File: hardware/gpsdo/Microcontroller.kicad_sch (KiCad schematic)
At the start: 31 parts, among them J1 Conn_01x02, J2 Conn_02x03_Top_Bottom, J3 USB_C_Receptacle_USB2.0_14P, U6 STM32F411CEUx, U7 AMS1117-3.3, X1 X322516MLB4SI

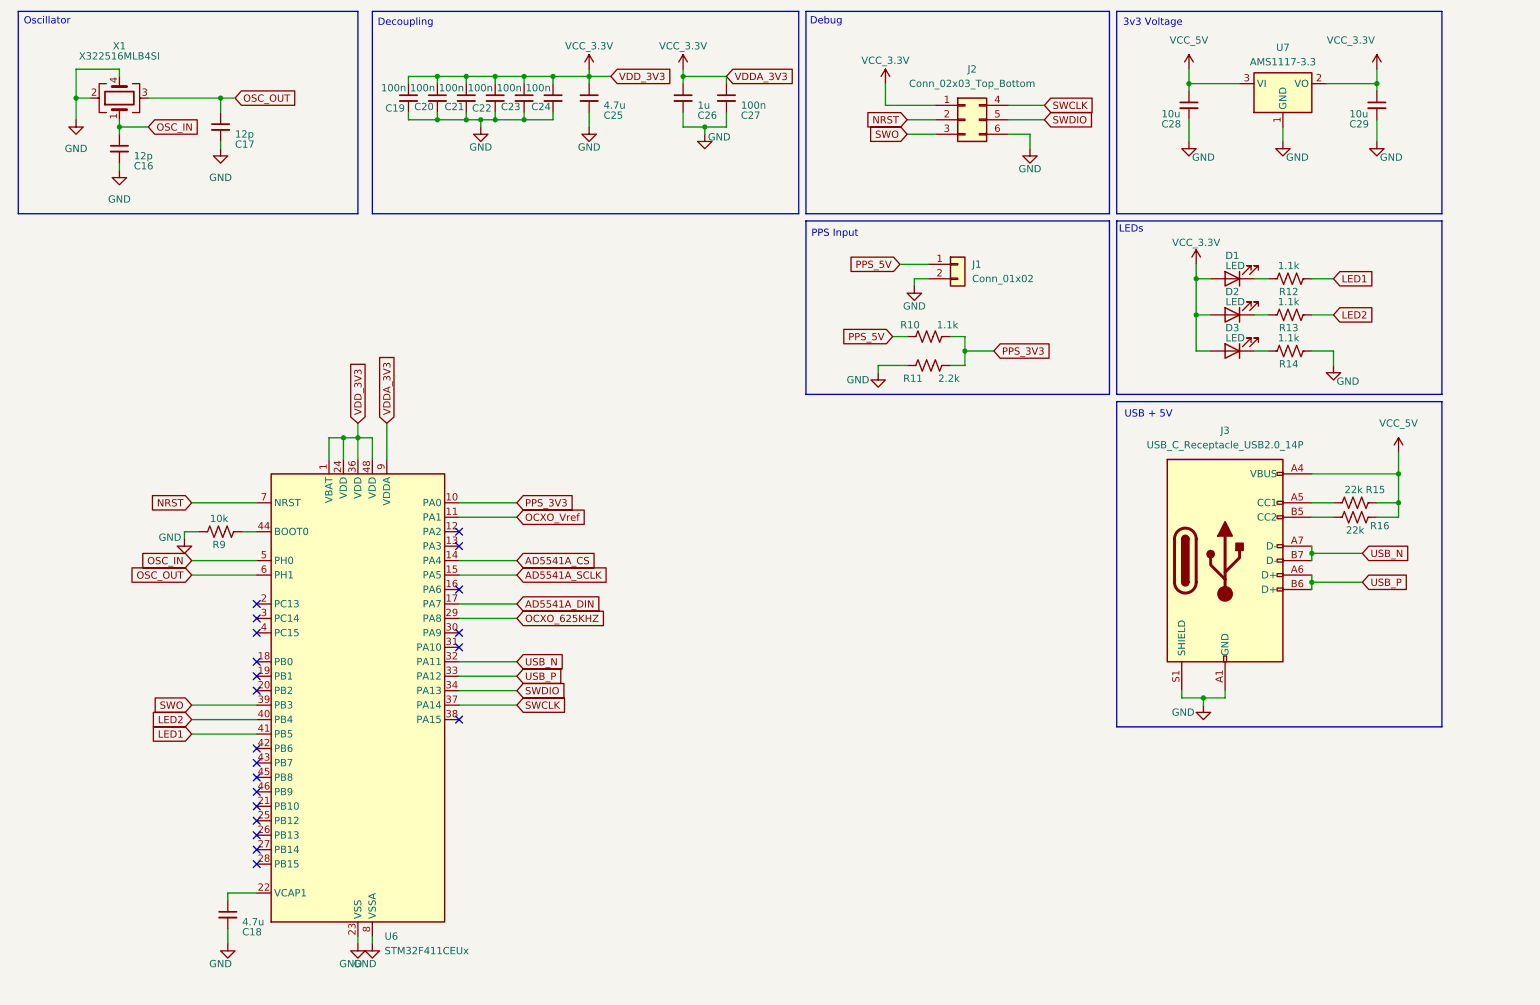
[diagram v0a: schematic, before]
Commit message: update hal; update schematics and routing
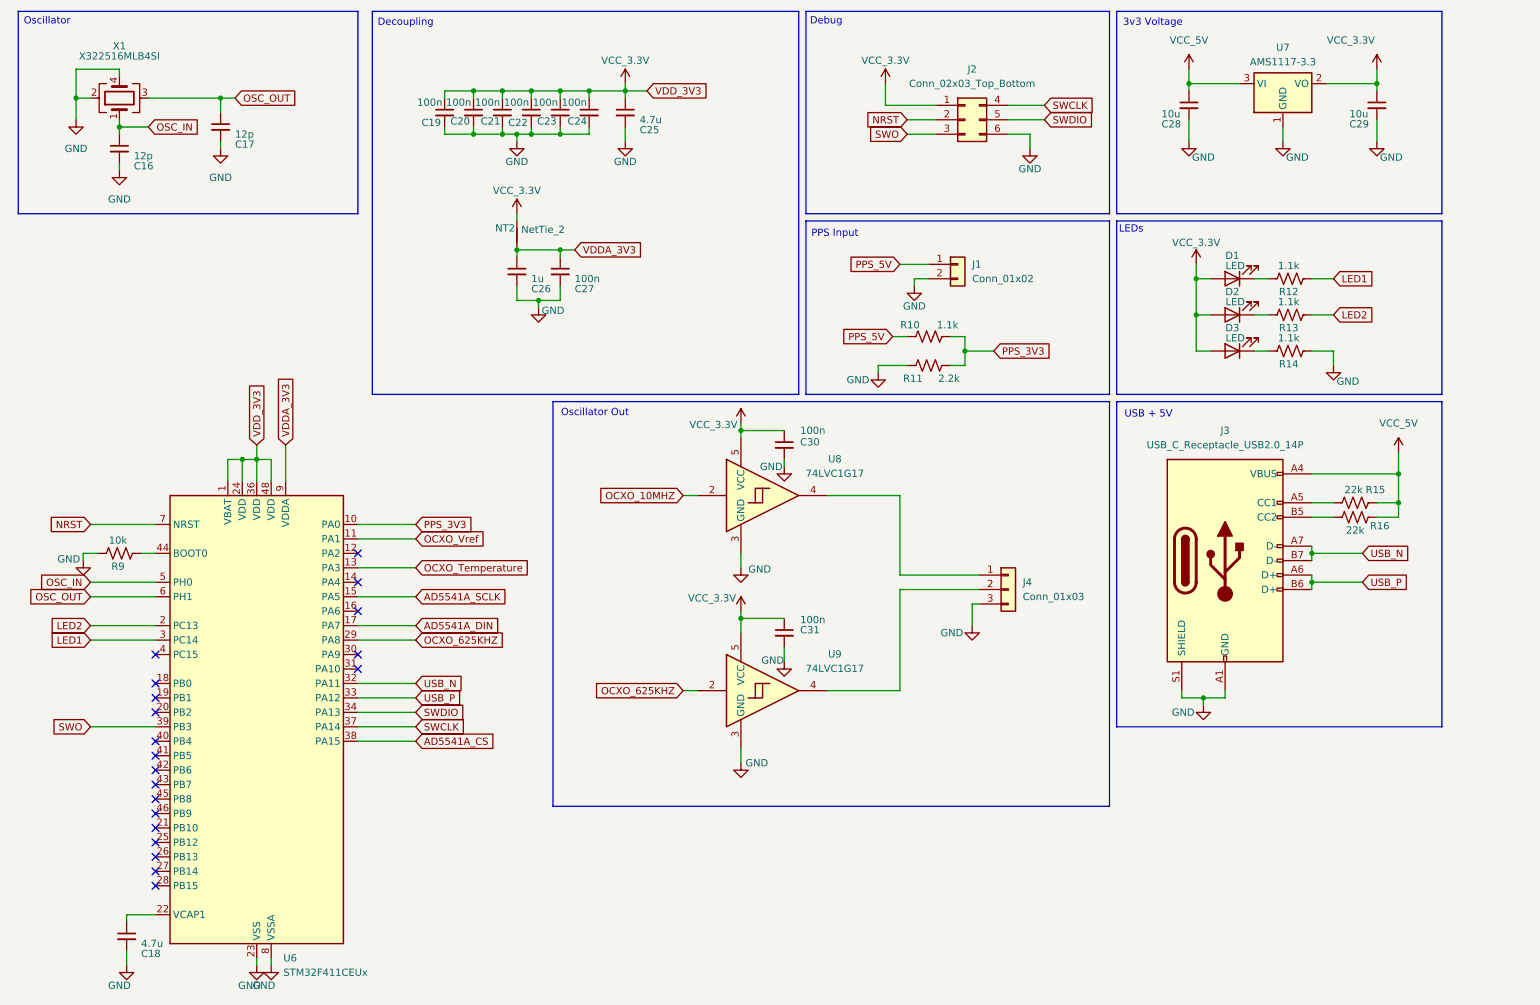
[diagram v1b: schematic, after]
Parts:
- added C30, C31: 100n, Capacitor_SMD:C_0201_0603Metric_Pad0.64x0.40mm_HandSolder, symbol Device:C_Small
- added J4: Conn_01x03, Connector_PinHeader_2.54mm:PinHeader_1x03_P2.54mm_Vertical, symbol Connector_Generic:Conn_01x03
- added NT2: NetTie_2, NetTie:NetTie-2_THT_Pad0.3mm, symbol Device:NetTie_2
- added U8, U9: 74LVC1G17, Package_TO_SOT_SMD:SOT-23-5, symbol 74xGxx:74LVC1G17
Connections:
- net AD5541A_CS: now also U6.38 (PA15); no longer U6.14 (PA4)
- net GND: now also C30.2, C31.2, J4.3 (Pin_3), U8.3 (GND), U9.3 (GND)
- net LED1: now also U6.3 (PC14); no longer U6.41 (PB5)
- net LED2: now also U6.2 (PC13); no longer U6.40 (PB4)
- net OCXO_625KHZ: now also U9.2
- net VCC_3.3V: now also C30.1, C31.1, NT2.2, U8.5 (VCC), U9.5 (VCC); no longer C26.1, C27.1, U6.9 (VDDA)
- net OCXO_Temperature: now reaches U6.13 (PA3)
- new net: J4.1 (Pin_1), U8.4
- new net: J4.2 (Pin_2), U9.4
- new net OCXO_10MHZ: U8.2
- new net VDDA_3V3: C26.1, C27.1, NT2.1, U6.9 (VDDA)
- no-connect marks 21 -> 20
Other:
- note added: "Oscillator Out"
- moved on the sheet: C18, C19, C20, C21, C22, C23, C24, C25, C26, C27, R9, U6

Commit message: update routing
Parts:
- removed U8, U9: 74LVC1G17, Package_TO_SOT_SMD:SOT-23-5, symbol 74xGxx:74LVC1G17
- added C33, C34, C35, C37: 100n, Capacitor_SMD:C_0201_0603Metric_Pad0.64x0.40mm_HandSolder, symbol Device:C_Small
- added C36: 1u, Capacitor_SMD:C_0201_0603Metric_Pad0.64x0.40mm_HandSolder, symbol Device:C_Small
- added J5: Conn_Coaxial, Connector_Coaxial:SMA_Samtec_SMA-J-P-H-ST-EM1_EdgeMount, symbol Connector:Conn_Coaxial
- added R18: 33, Resistor_SMD:R_0201_0603Metric_Pad0.64x0.40mm_HandSolder, symbol Device:R_US
- added TP2: TestPoint, TestPoint:TestPoint_Pad_D1.0mm, symbol Connector:TestPoint
- added U9: SN74LVC1G125DBV, Package_TO_SOT_SMD:SOT-23-5, symbol 74xGxx:SN74LVC1G125DBV
- C30: value 100n -> 10u
- U6: JLC (none) -> C60420
- U7: JLC (none) -> C347222
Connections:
- net GND: now also C33.2, C34.2, C35.2
- net OCXO_10MHZ: now also J4.1 (Pin_1)
- net OCXO_625KHZ: now also J4.2 (Pin_2)
- net VCC_3.3V: now also C33.1
- net VCC_5V: now also C34.1, C35.1, C36.1, C37.1, U9.5 (VCC)
- new net: J5.1 (In), R18.1, TP2.1
- new net: R18.2, U9.4
- new net GNDA: C36.2, C37.2, J5.2 (Ext), U9.3 (GND)
- new net OCXO_Out: U9.1, U9.2
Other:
- note added: "Oscillator SMA"
- moved on the sheet: J3, J4, R15, R16

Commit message: update routing; bugfix in downsampling; replace voltage dividers with level shifter
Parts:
- removed J4: Conn_01x03, Connector_PinHeader_2.54mm:PinHeader_1x03_P2.54mm_Vertical, symbol Connector_Generic:Conn_01x03
- removed R10: 1.1k, Resistor_SMD:R_0201_0603Metric_Pad0.64x0.40mm_HandSolder, symbol Device:R_US
- removed R11: 2.2k, Resistor_SMD:R_0201_0603Metric_Pad0.64x0.40mm_HandSolder, symbol Device:R_US
- added C2, C40: 100n, Capacitor_SMD:C_0201_0603Metric_Pad0.64x0.40mm_HandSolder, symbol Device:C_Small
- added J7: Conn_01x05, Connector_PinHeader_2.54mm:PinHeader_1x05_P2.54mm_Vertical, symbol Connector_Generic:Conn_01x05
- added U2: SN74LVC1T45DCK, Package_TO_SOT_SMD:SOT-363_SC-70-6, symbol Logic_LevelTranslator:SN74LVC1T45DCK
- C16, C17: JLC (none) -> C38523; Package (none) -> 0603
- C18, C25: JLC (none) -> C19666; Package (none) -> 0603
- C19, C20, C21, C22, C23, C24, C27, C31, C33, C34, C35, C37: JLC (none) -> C14663; Package (none) -> 0603
- C26, C36: JLC (none) -> C15849; Package (none) -> 0603
- C28, C29, C30: JLC (none) -> C19702; Package (none) -> 0603
- D1: JLC (none) -> C2296; Package (none) -> 0805
- D2: JLC (none) -> C84256; Package (none) -> 0805
- D3: JLC (none) -> C2297; Package (none) -> 0805
- J1, J2, J5, TP2: now left out of the parts list
- R12, R13, R14: JLC (none) -> C17375; Package (none) -> 0603
- R15, R16: JLC (none) -> C31850; Package (none) -> 0603
- R18: JLC (none) -> C23140; Package (none) -> 0603
- R9: JLC (none) -> C25804; Package (none) -> 0603
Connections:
- net GND: now also C2.2, C40.2, J7.5 (Pin_5), U2.2 (GND), U2.5 (DIR)
- net OCXO_625KHZ: now also J7.4 (Pin_4); no longer U6.29 (PA8)
- net PPS_3V3: now also U2.3 (A)
- net PPS_5V: now also U2.4 (B)
- net VCC_3.3V: now also C40.1, U2.1 (VCCA)
- net VCC_5V: now also C2.1, U2.6 (VCCB)
- new net OCXO_1.25MHZ: J7.3 (Pin_3)
- new net OCXO_2.5MHZ: J7.2 (Pin_2)
- new net OCXO_5MHZ: J7.1 (Pin_1)
- new net OCXO_625KHZ_3V3: U6.29 (PA8)
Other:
- moved on the sheet: C34, C35, C36, C37, D1, D2, D3, J3, J5, R12, R13, R14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

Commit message: bugfix in bom
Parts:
- U2: JLC (none) -> C9382

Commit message: revisit footprints
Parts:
- C16, C17, C18, C19, C2, C20, C21, C22, C23, C24, C25, C26, C27, C28, C29, C30, C31, C33, C34, C35, C36, C37, C40: footprint Capacitor_SMD:C_0201_0603Metric_Pad0.64x0.40mm_HandSolder -> Capacitor_SMD:C_0603_1608Metric
- R12, R13, R14, R15, R16, R18, R9: footprint Resistor_SMD:R_0201_0603Metric_Pad0.64x0.40mm_HandSolder -> Resistor_SMD:R_0603_1608Metric
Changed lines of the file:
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@@
 			)
 		)
-		(property "Footprint" "Capacitor_SMD:C_0201_0603Metric_Pad0.64x0.40mm_HandSolder"
+		(property "Footprint" "Capacitor_SMD:C_0603_1608Metric"
 			(at 113.03 64.77 0)
 			(effects
@@
 			)
 		)
-		(property "Footprint" "Capacitor_SMD:C_0201_0603Metric_Pad0.64x0.40mm_HandSolder"
+		(property "Footprint" "Capacitor_SMD:C_0603_1608Metric"
 			(at 105.41 64.77 0)
 			(effects
@@
 			)
 		)
-		(property "Footprint" "Capacitor_SMD:C_0201_0603Metric_Pad0.64x0.40mm_HandSolder"
+		(property "Footprint" "Capacitor_SMD:C_0603_1608Metric"
 			(at 35.56 43.18 0)
 			(effects
@@
 			)
 		)
-		(property "Footprint" "Capacitor_SMD:C_0201_0603Metric_Pad0.64x0.40mm_HandSolder"
+		(property "Footprint" "Capacitor_SMD:C_0603_1608Metric"
 			(at 118.11 36.83 0)
 			(effects
@@
 			)
 		)
-		(property "Footprint" "Capacitor_SMD:C_0201_0603Metric_Pad0.64x0.40mm_HandSolder"
+		(property "Footprint" "Capacitor_SMD:C_0603_1608Metric"
 			(at 271.78 35.56 0)
 			(effects
@@
 			)
 		)
-		(property "Footprint" "Resistor_SMD:R_0201_0603Metric_Pad0.64x0.40mm_HandSolder"
+		(property "Footprint" "Resistor_SMD:R_0603_1608Metric"
 			(at 180.086 125.476 90)
 			(effects
@@
 			)
 		)
-		(property "Footprint" "Resistor_SMD:R_0201_0603Metric_Pad0.64x0.40mm_HandSolder"
+		(property "Footprint" "Resistor_SMD:R_0603_1608Metric"
 			(at 35.306 115.316 90)
 			(effects
@@
 			)
 		)
-		(property "Footprint" "Capacitor_SMD:C_0201_0603Metric_Pad0.64x0.40mm_HandSolder"
+		(property "Footprint" "Capacitor_SMD:C_0603_1608Metric"
 			(at 261.62 35.56 0)
 			(effects
@@
 			)
 		)
-		(property "Footprint" "Capacitor_SMD:C_0201_0603Metric_Pad0.64x0.40mm_HandSolder"
+		(property "Footprint" "Capacitor_SMD:C_0603_1608Metric"
 			(at 102.87 36.83 0)
 			(effects
@@
 			)
 		)
-		(property "Footprint" "Capacitor_SMD:C_0201_0603Metric_Pad0.64x0.40mm_HandSolder"
+		(property "Footprint" "Capacitor_SMD:C_0603_1608Metric"
 			(at 53.34 39.37 0)
 			(effects
@@
 			)
 		)
-		(property "Footprint" "Capacitor_SMD:C_0201_0603Metric_Pad0.64x0.40mm_HandSolder"
+		(property "Footprint" "Capacitor_SMD:C_0603_1608Metric"
 			(at 256.54 35.56 0)
 			(effects
@@
 			)
 		)
-		(property "Footprint" "Capacitor_SMD:C_0201_0603Metric_Pad0.64x0.40mm_HandSolder"
+		(property "Footprint" "Capacitor_SMD:C_0603_1608Metric"
 			(at 124.46 36.83 0)
 			(effects
@@
 			)
 		)
-		(property "Footprint" "Capacitor_SMD:C_0201_0603Metric_Pad0.64x0.40mm_HandSolder"
+		(property "Footprint" "Capacitor_SMD:C_0603_1608Metric"
 			(at 113.03 36.83 0)
 			(effects
@@
 			)
 		)
-		(property "Footprint" "Capacitor_SMD:C_0201_0603Metric_Pad0.64x0.40mm_HandSolder"
+		(property "Footprint" "Capacitor_SMD:C_0603_1608Metric"
 			(at 97.79 36.83 0)
 			(effects
@@
 			)
 		)
-		(property "Footprint" "Capacitor_SMD:C_0201_0603Metric_Pad0.64x0.40mm_HandSolder"
+		(property "Footprint" "Capacitor_SMD:C_0603_1608Metric"
 			(at 223.52 35.56 0)
 			(effects
@@
 			)
 		)
-		(property "Footprint" "Capacitor_SMD:C_0201_0603Metric_Pad0.64x0.40mm_HandSolder"
+		(property "Footprint" "Capacitor_SMD:C_0603_1608Metric"
 			(at 228.6 66.04 0)
 			(effects
@@
 			)
 		)
-		(property "Footprint" "Resistor_SMD:R_0201_0603Metric_Pad0.64x0.40mm_HandSolder"
+		(property "Footprint" "Resistor_SMD:R_0603_1608Metric"
 			(at 48.006 73.406 90)
 			(effects
@@
 			)
 		)
-		(property "Footprint" "Resistor_SMD:R_0201_0603Metric_Pad0.64x0.40mm_HandSolder"
+		(property "Footprint" "Resistor_SMD:R_0603_1608Metric"
 			(at 48.006 79.756 90)
 			(effects
@@
 			)
 		)
-		(property "Footprint" "Resistor_SMD:R_0201_0603Metric_Pad0.64x0.40mm_HandSolder"
+		(property "Footprint" "Resistor_SMD:R_0603_1608Metric"
 			(at 48.006 67.056 90)
 			(effects
@@
 			)
 		)
-		(property "Footprint" "Capacitor_SMD:C_0201_0603Metric_Pad0.64x0.40mm_HandSolder"
+		(property "Footprint" "Capacitor_SMD:C_0603_1608Metric"
 			(at 266.7 35.56 0)
 			(effects
@@
 			)
 		)
-		(property "Footprint" "Resistor_SMD:R_0201_0603Metric_Pad0.64x0.40mm_HandSolder"
+		(property "Footprint" "Resistor_SMD:R_0603_1608Metric"
 			(at 251.206 121.666 90)
 			(effects
@@
 			)
 		)
-		(property "Footprint" "Resistor_SMD:R_0201_0603Metric_Pad0.64x0.40mm_HandSolder"
+		(property "Footprint" "Resistor_SMD:R_0603_1608Metric"
 			(at 251.206 124.206 90)
 			(effects
@@
 			)
 		)
-		(property "Footprint" "Capacitor_SMD:C_0201_0603Metric_Pad0.64x0.40mm_HandSolder"
+		(property "Footprint" "Capacitor_SMD:C_0603_1608Metric"
 			(at 36.83 181.61 0)
 			(effects
@@
 			)
 		)
-		(property "Footprint" "Capacitor_SMD:C_0201_0603Metric_Pad0.64x0.40mm_HandSolder"
+		(property "Footprint" "Capacitor_SMD:C_0603_1608Metric"
 			(at 107.95 36.83 0)
 			(effects
@@
 			)
 		)
-		(property "Footprint" "Capacitor_SMD:C_0201_0603Metric_Pad0.64x0.40mm_HandSolder"
+		(property "Footprint" "Capacitor_SMD:C_0603_1608Metric"
 			(at 92.71 36.83 0)
 			(effects
@@
 			)
 		)
-		(property "Footprint" "Capacitor_SMD:C_0201_0603Metric_Pad0.64x0.40mm_HandSolder"
+		(property "Footprint" "Capacitor_SMD:C_0603_1608Metric"
 			(at 275.59 119.38 0)
 			(effects
@@
 			)
 		)
-		(property "Footprint" "Capacitor_SMD:C_0201_0603Metric_Pad0.64x0.40mm_HandSolder"
+		(property "Footprint" "Capacitor_SMD:C_0603_1608Metric"
 			(at 142.24 113.03 0)
 			(effects
@@
 			)
 		)
-		(property "Footprint" "Capacitor_SMD:C_0201_0603Metric_Pad0.64x0.40mm_HandSolder"
+		(property "Footprint" "Capacitor_SMD:C_0603_1608Metric"
 			(at 241.3 66.04 0)
 			(effects
@@
 			)
 		)
-		(property "Footprint" "Capacitor_SMD:C_0201_0603Metric_Pad0.64x0.40mm_HandSolder"
+		(property "Footprint" "Capacitor_SMD:C_0603_1608Metric"
 			(at 267.97 119.38 0)
 			(effects
@@
 			)
 		)
-		(property "Footprint" "Capacitor_SMD:C_0201_0603Metric_Pad0.64x0.40mm_HandSolder"
+		(property "Footprint" "Capacitor_SMD:C_0603_1608Metric"
 			(at 134.62 113.03 0)
 			(effects
